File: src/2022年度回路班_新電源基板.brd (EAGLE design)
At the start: 112.7 x 77 mm, 46 parts

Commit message: 配線完了
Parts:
- flipped R5 to the top, turned to 180 degrees
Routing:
- net N$20: track 86.6 -> 85.2 mm
- net GND: track 61.3 -> 62.2 mm
- net N$19: track 93.5 -> 94.3 mm
- net N$21: track 92.6 -> 92.0 mm
- net PWM3: track 30.1 -> 29.6 mm
- net N$3: track 6.13 -> 6.12 mm, vias 0 -> 1

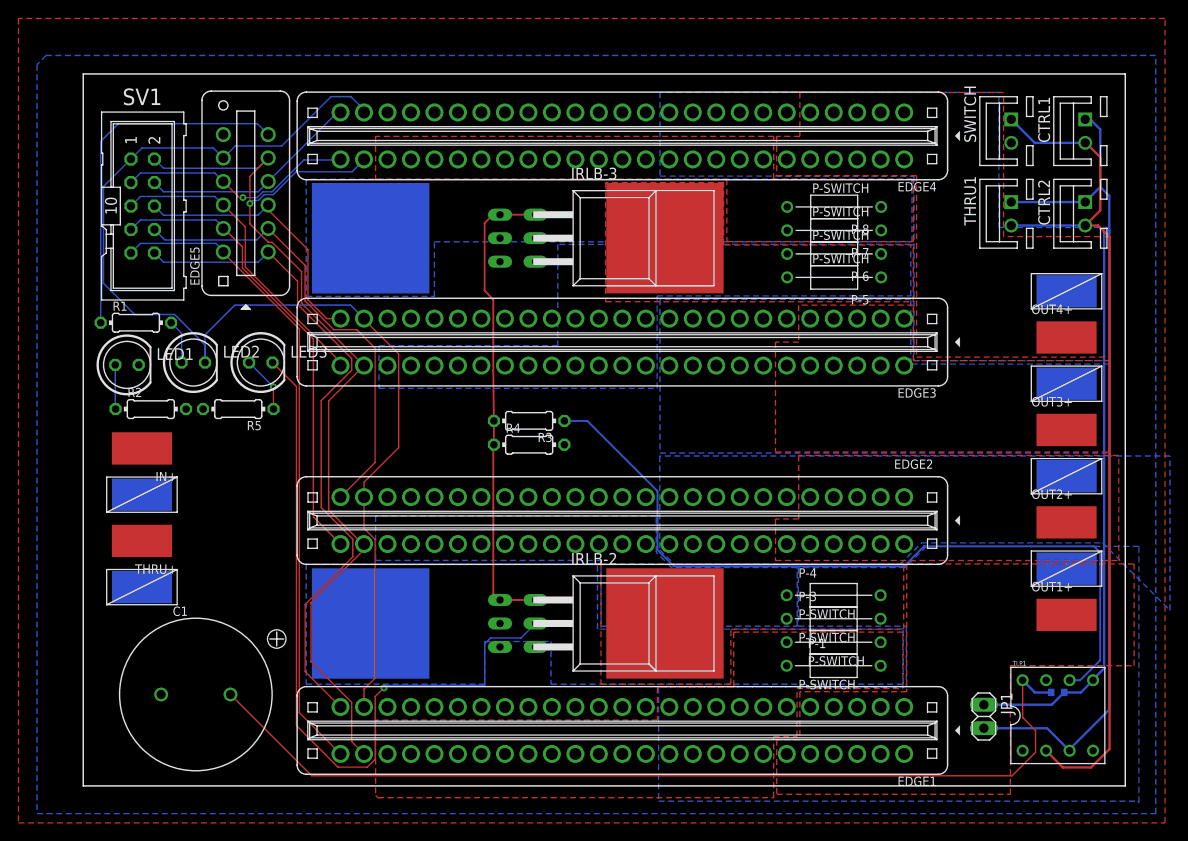
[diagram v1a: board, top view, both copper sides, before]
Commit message: 配線完了,KiCadへの移行の前段階
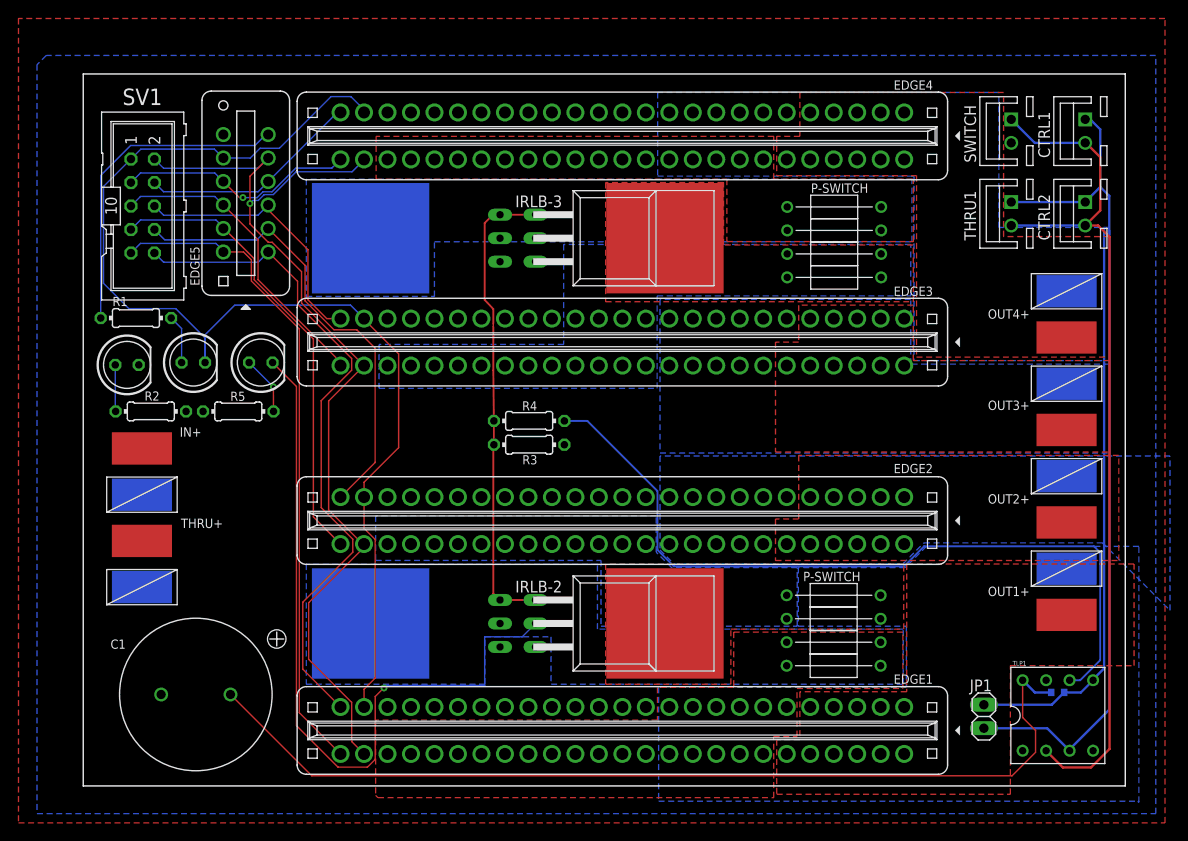
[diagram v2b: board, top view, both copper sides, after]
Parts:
- moved R1 0.51 mm to (5.70, 50.6)
- moved R2 0.25 mm to (7.31, 40.5)
- moved R5 0.25 mm to (16.8, 40.5)
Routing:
- net LED: track 39.0 -> 35.4 mm
- net DIR1: track 70.4 -> 71.7 mm
- net N$18: track 4.77 -> 5.28 mm
